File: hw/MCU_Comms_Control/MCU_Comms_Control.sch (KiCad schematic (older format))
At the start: 8 parts

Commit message: continue digital design
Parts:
- removed J?: CAN BUS, symbol Connector:DB9_Female
- removed JP?: CAN_GND_TIE, symbol Jumper:SolderJumper_2_Open
- removed U?: SN65HVD232, Package_SO:SOIC-8_3.9x4.9mm_P1.27mm, symbol Interface_CAN_LIN:SN65HVD232
- added D? (x2): 1N5819, Diode_THT:D_DO-41_SOD81_P10.16mm_Horizontal, symbol Diode:1N5819
- added J?: CAN BUS, symbol Connector_Generic:Conn_02x04_Top_Bottom
- added J?: TO_POWER_BOARD, symbol Connector_Generic:Conn_02x13_Top_Bottom
- added J?: USB_B_Mini, symbol Connector:USB_B_Mini
- added J?: Mini-Debugging, symbol Connector_Generic:Conn_02x05_Odd_Even
- added R?: 0, symbol Device:R_Small
- added R? (x2): 4k7, symbol Device:R_Small
- added R?: 1k5, symbol Device:R_Small
- added R?: 120, symbol Device:R_Small
- added U?: SN65HVD230, Package_SO:SOIC-8_3.9x4.9mm_P1.27mm, symbol Interface_CAN_LIN:SN65HVD230
- added U?: W25Q128JVS, Package_SO:SOIC-8_5.23x5.23mm_P1.27mm, symbol Memory_Flash:W25Q128JVS
- added U?: SRV05-4, Package_TO_SOT_SMD:SOT-23-6, symbol Power_Protection:SRV05-4
- added U?: EL817, Package_DIP:DIP-4_W7.62mm, symbol Isolator:EL817
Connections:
- net labels added: +5V, CAN_RX, CAN_TX, ENABLE, ERR_OUT, FLASH_CLK, FLASH_MISO, FLASH_MOSI, GPIO1, GPIO2, GPIO3, HALL1, HALL2, HALL3, SWCLK, SWDIO, SWO, USB_DM, USB_DP, U_H, U_L, VBUS_SCALED, V_H, V_L, W_H, W_L, ~ERROR, ~FLASH_CS, ~RESET
- wire segments 45 -> 75
- no-connect marks 0 -> 4
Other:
- note added: "Pull-up resistor for\nfull-speed identification\nTied to SWDIO for\neasier routing"
- note added: "RESERVED"
- note added: "We don't care \nabout EMI for now"
- note removed: "CAN shield ground"
- note removed: "Power GND"
- note removed: "This footprint lacks\nthe Rs pin....."
- moved on the sheet: C?, R?, U?, Y?

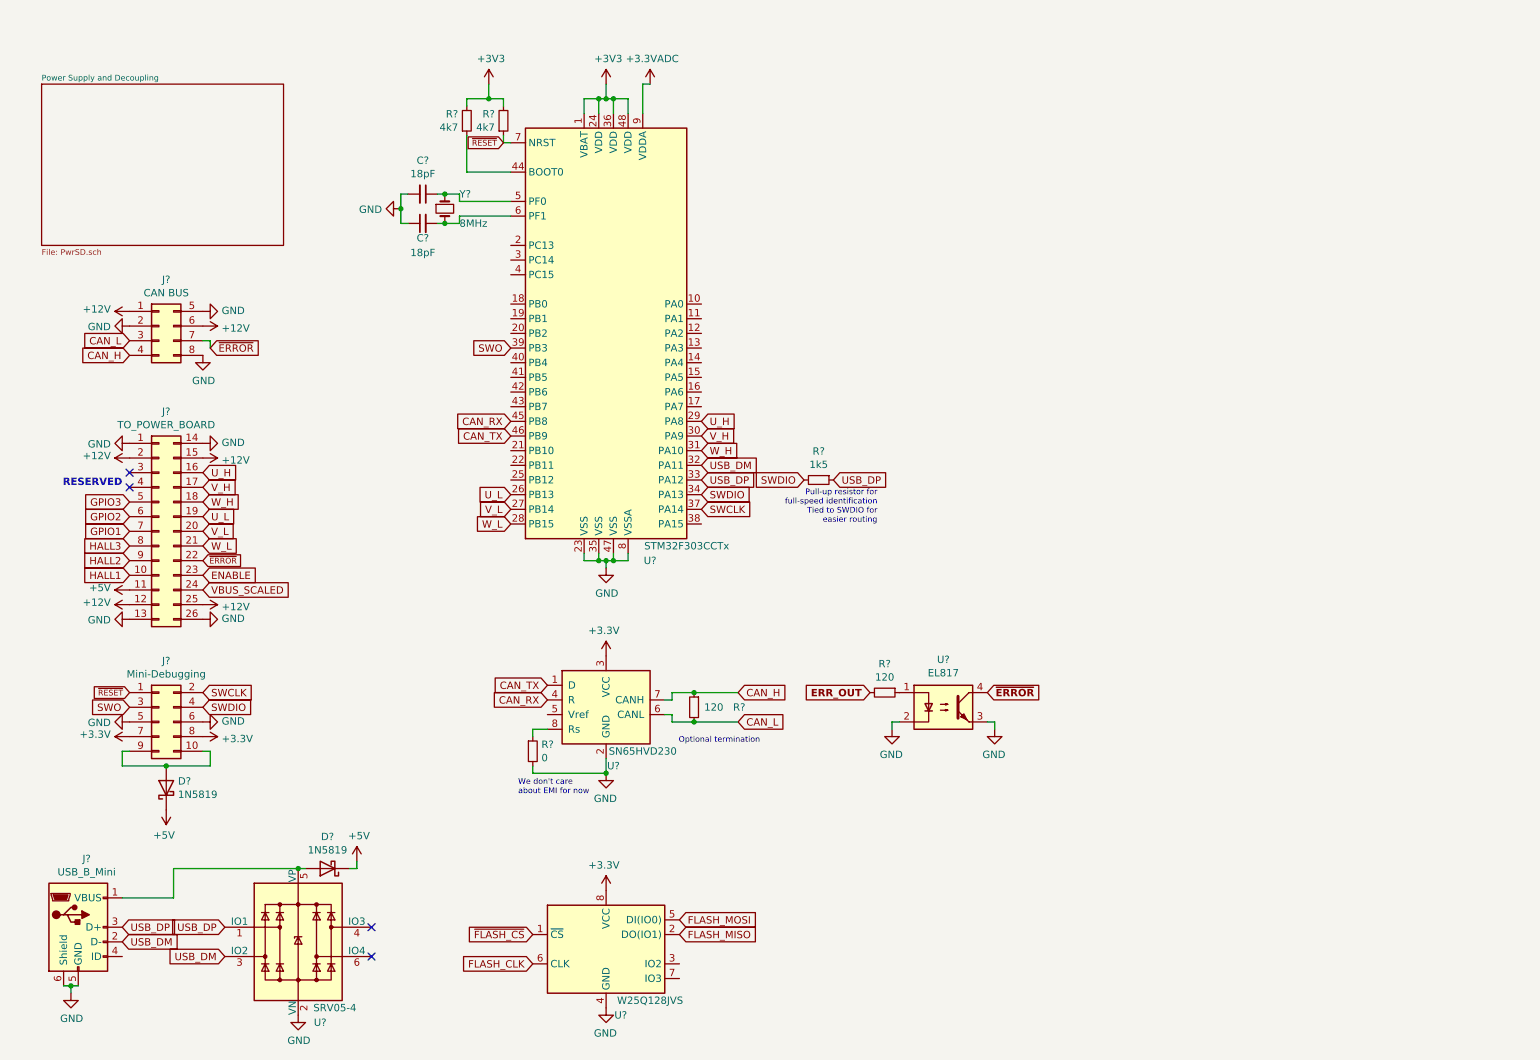
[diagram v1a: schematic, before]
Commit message: finish schematic of mcu/comms and start review process
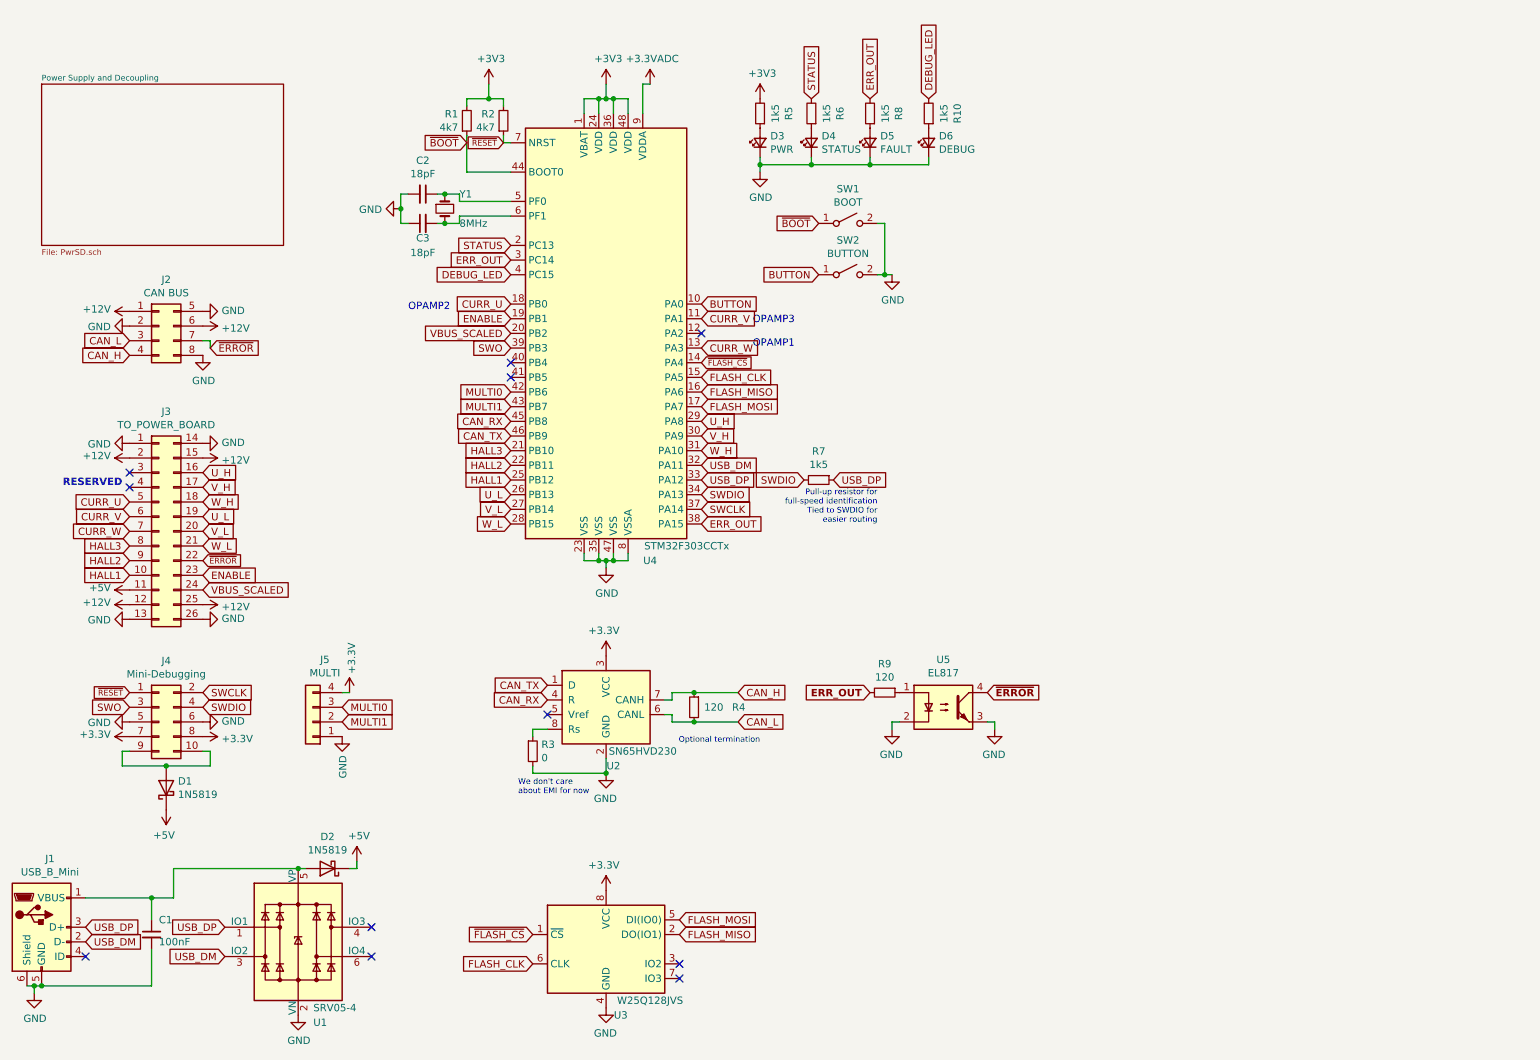
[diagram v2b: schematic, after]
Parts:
- added C1: 100nF, symbol Device:C_Small
- added D3: PWR, symbol Device:LED_Small
- added D4: STATUS, symbol Device:LED_Small
- added D5: FAULT, symbol Device:LED_Small
- added D6: DEBUG, symbol Device:LED_Small
- added J5: MULTI, symbol Connector_Generic:Conn_01x04
- added R10, R5, R6, R8: 1k5, symbol Device:R_Small
- added SW1: BOOT, symbol Switch:SW_SPST
- added SW2: BUTTON, symbol Switch:SW_SPST
- gave numbers to parts that had none: 20
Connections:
- net GPIO1 is gone; now on net CURR_W: J3.7 (Pin_7)
- net GPIO2 is gone; now on net CURR_V: J3.6 (Pin_6)
- net GPIO3 is gone; now on net CURR_U: J3.5 (Pin_5)
- net +3V3: now also J5.4 (Pin_4), R5.2
- net ENABLE: now also U4.19 (PB1)
- net ERR_OUT: now also U4.3 (PC14), U4.38 (PA15), R8.2
- net FLASH_CLK: now also U4.15 (PA5)
- net FLASH_MISO: now also U4.16 (PA6)
- net FLASH_MOSI: now also U4.17 (PA7)
- net GND: now also C1.2, D3.1 (K), D4.1 (K), D5.1 (K), D6.1 (K), J5.1 (Pin_1), SW1.2 (B), SW2.2 (B)
- net HALL1: now also U4.25 (PB12)
- net HALL2: now also U4.22 (PB11)
- net HALL3: now also U4.21 (PB10)
- net VBUS_SCALED: now also U4.20 (PB2)
- net ~FLASH_CS: now also U4.14 (PA4)
- net BUTTON: now reaches U4.10 (PA0)
- net BUTTON: now also SW2.1 (A)
- net CURR_V: now reaches U4.11 (PA1)
- net CURR_W: now reaches U4.13 (PA3)
- net CURR_U: now reaches U4.18 (PB0)
- net STATUS: now reaches U4.2 (PC13)
- net STATUS: now also R6.2
- net DEBUG_LED: now reaches U4.4 (PC15)
- net DEBUG_LED: now also R10.2
- net MULTI0: now reaches U4.42 (PB6)
- net MULTI0: now also J5.3 (Pin_3)
- net MULTI1: now reaches U4.43 (PB7)
- net MULTI1: now also J5.2 (Pin_2)
- net ~BOOT: now reaches R1.1, U4.44 (BOOT0)
- net ~BOOT: now also SW1.1 (A)
- net at D2.2 (A), J1.1 (VBUS), U1.5 (VP): now also C1.1
- new net: D3.2 (A), R5.1
- new net: D4.2 (A), R6.1
- new net: D5.2 (A), R8.1
- new net: D6.2 (A), R10.1
- no-connect marks 4 -> 11
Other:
- note added: "OPAMP2\n"
- note added: "OPAMP3\n\nOPAMP1"
- moved on the sheet: J1

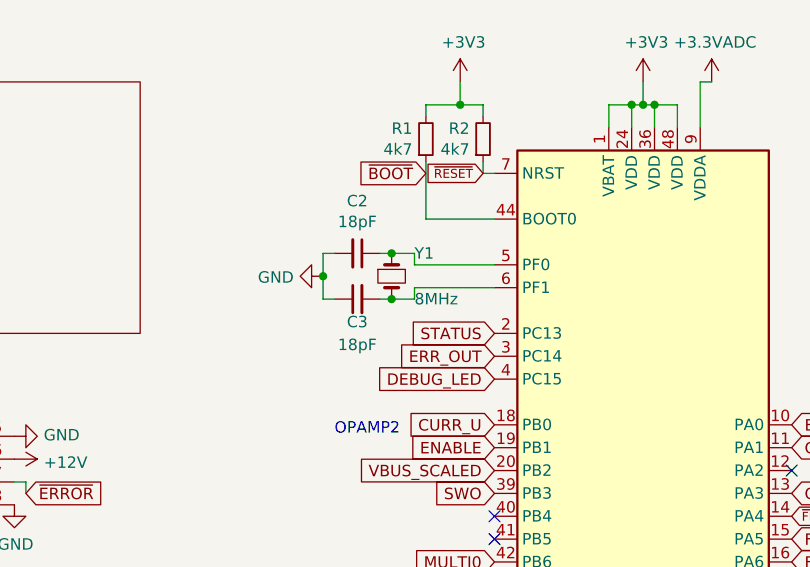
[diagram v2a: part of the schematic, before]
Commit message: add footprints and lcsc code
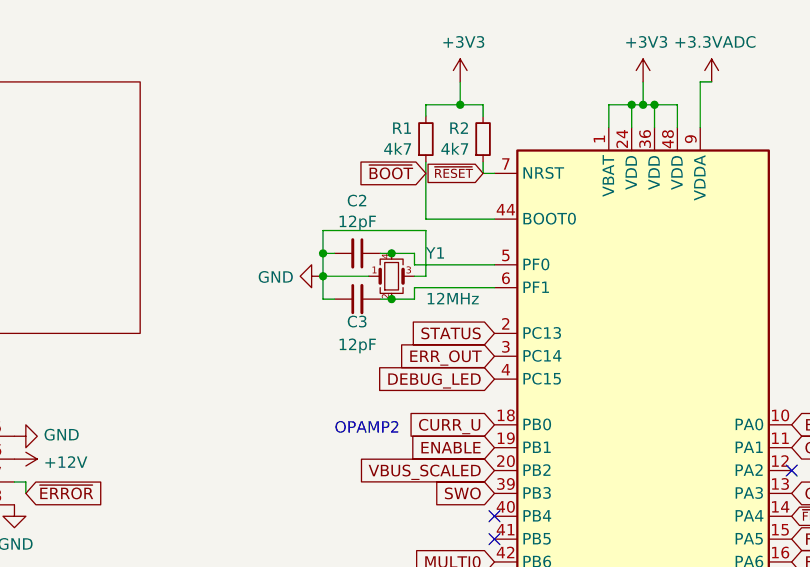
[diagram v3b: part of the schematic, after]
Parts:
- removed Y1: 8MHz, symbol Device:Crystal_Small
- added Y1: 12MHz, Crystal:Crystal_SMD_3225-4Pin_3.2x2.5mm, symbol Device:Crystal_GND24_Small
- C1: footprint (none) -> Capacitor_SMD:C_0603_1608Metric; LCSC (none) -> C14663
- C2, C3: value 18pF -> 12pF; footprint (none) -> Capacitor_SMD:C_0603_1608Metric; LCSC (none) -> C38523
- D1, D2: footprint Diode_THT:D_DO-41_SOD81_P10.16mm_Horizontal -> Diode_SMD:D_SOD-123; LCSC (none) -> C8598
- D3: footprint (none) -> LED_SMD:LED_0603_1608Metric_Castellated; LCSC (none) -> C72043
- D4, D6: footprint (none) -> LED_SMD:LED_0603_1608Metric_Castellated; LCSC (none) -> C72038
- D5: footprint (none) -> LED_SMD:LED_0603_1608Metric_Castellated; LCSC (none) -> C2286
- J1: footprint (none) -> Connector_USB:USB_Micro-B_Molex-105017-0001
- J2: footprint (none) -> Connector_Molex:Molex_Mini-Fit_Jr_5566-08A_2x04_P4.20mm_Vertical
- J3: footprint (none) -> Connector_IDC:IDC-Header_2x13_P2.54mm_Vertical
- J4: footprint (none) -> Connector_PinHeader_2.54mm:PinHeader_2x05_P2.54mm_Vertical
- J5: footprint (none) -> Connector_PinHeader_2.54mm:PinHeader_1x04_P2.54mm_Vertical
- R1, R2: footprint (none) -> Resistor_SMD:R_0603_1608Metric; LCSC (none) -> C23162
- R10, R5, R6, R7, R8: footprint (none) -> Resistor_SMD:R_0603_1608Metric; LCSC (none) -> C22843
- R3: footprint (none) -> Resistor_SMD:R_0603_1608Metric; LCSC (none) -> C21189
- R4, R9: footprint (none) -> Resistor_SMD:R_0805_2012Metric; LCSC (none) -> C17437
- SW1, SW2: footprint (none) -> Button_Switch_SMD:SW_SPST_PTS645
- U1: LCSC (none) -> C85364
- U2: LCSC (none) -> C12084
- U3: LCSC (none) -> C97521
- U4: LCSC (none) -> C81523
- U5: footprint Package_DIP:DIP-4_W7.62mm -> Package_DIP:SMDIP-4_W7.62mm; LCSC (none) -> C106900
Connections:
- net GND: now also Y1.1, Y1.3
- net at C2.1, U4.5 (PF0): now also Y1.4
- net at C3.2, U4.6 (PF1): now also Y1.2
